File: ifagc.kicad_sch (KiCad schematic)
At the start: 39 parts, among them Q901 MMBFJ310, Q902 MMBFJ310, Q903 MMBT3904, Q904 MMBT3904, Q905 BSS138, T901 FT37-43

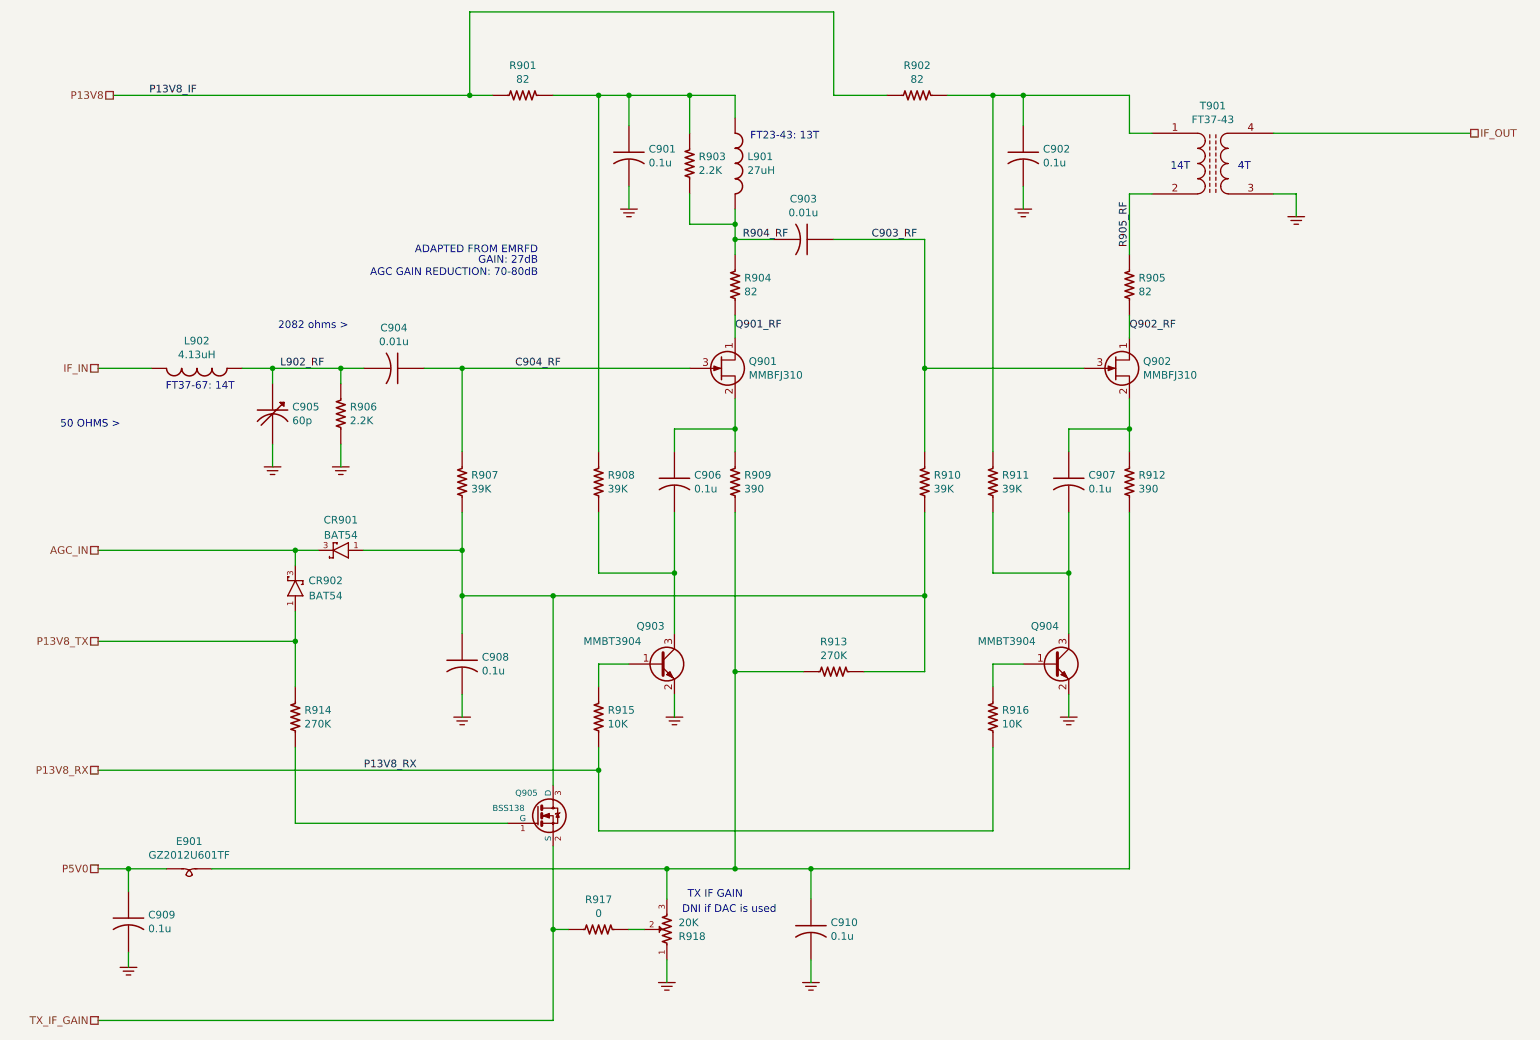
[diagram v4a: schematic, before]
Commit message: trx_mobo_concept_2_B. Change design to use a dedicated 8V supply for the 2SC3357 parts. Add S-Meter connector. Change mic connector to 3 pins and add 8V sopower supply to pin 3.
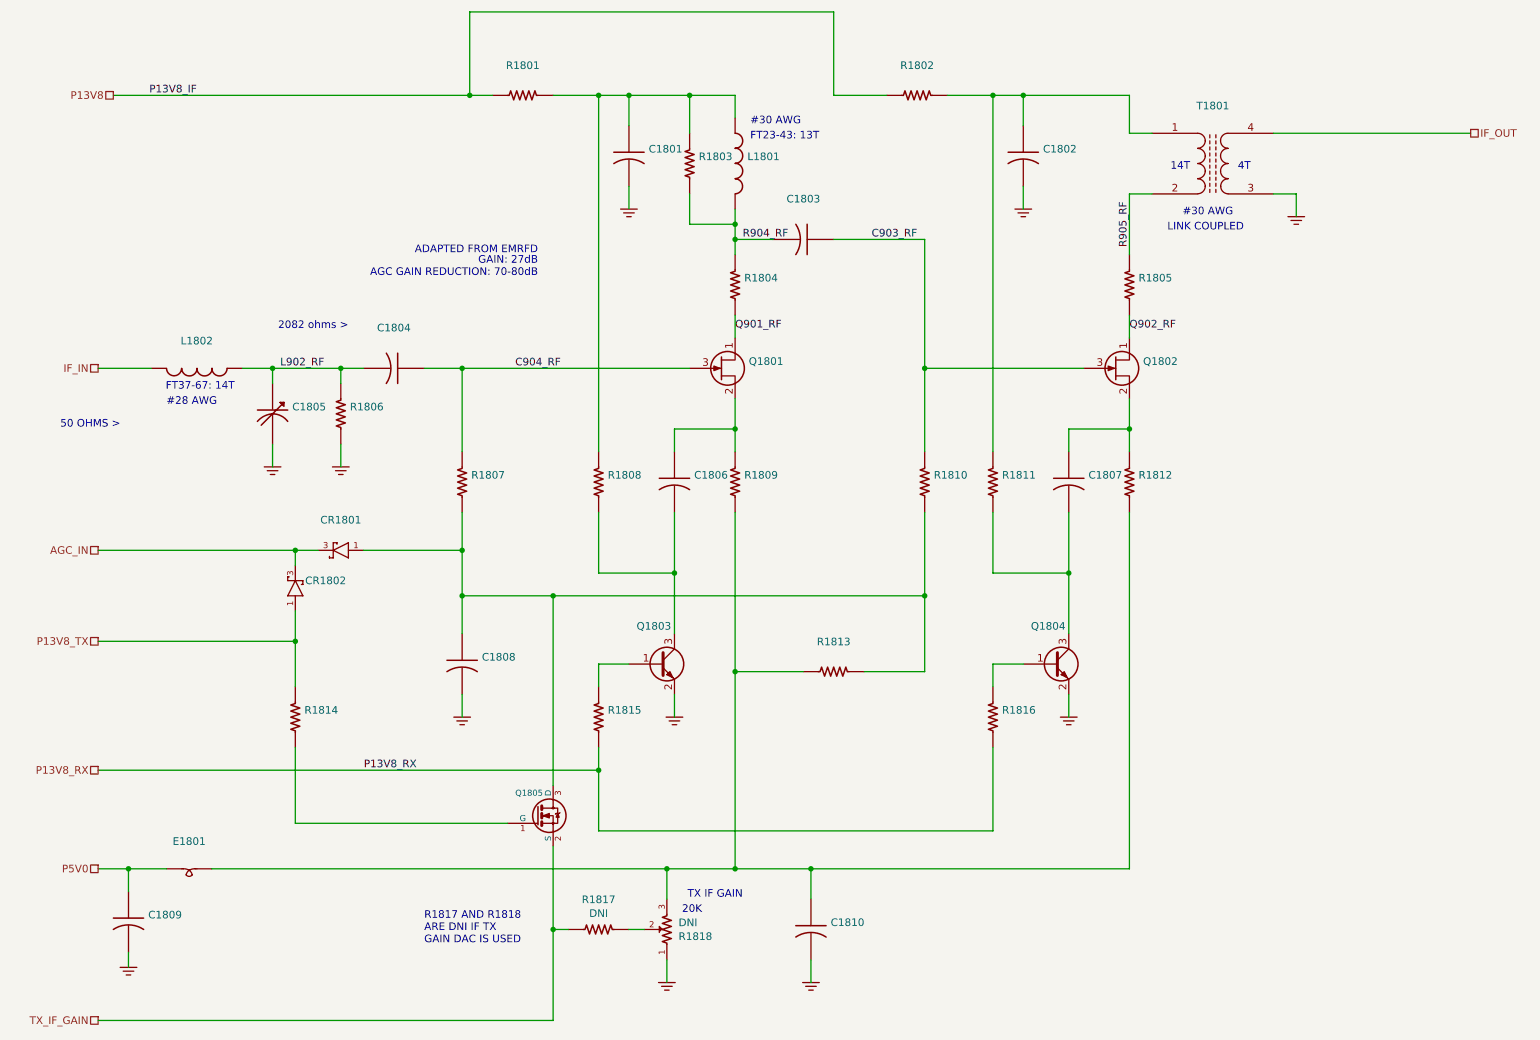
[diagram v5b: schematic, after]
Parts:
- C1801: renamed from C901; value 0.1u -> (none); footprint Capacitor_SMD:C_0805_2012Metric_Pad1.15x1.40mm_HandSolder -> (none)
- C1802: renamed from C902; value 0.1u -> (none); footprint Capacitor_SMD:C_0805_2012Metric_Pad1.15x1.40mm_HandSolder -> (none)
- C1803: renamed from C903; value 0.01u -> (none); footprint Capacitor_SMD:C_0805_2012Metric_Pad1.15x1.40mm_HandSolder -> (none)
- C1804: renamed from C904; value 0.01u -> (none); footprint Capacitor_SMD:C_0805_2012Metric_Pad1.15x1.40mm_HandSolder -> (none)
- C1805: renamed from C905; value 60p -> (none); footprint mods:Cap_Trimmer_THT_6mm_plastic -> (none)
- C1806: renamed from C906; value 0.1u -> (none); footprint Capacitor_SMD:C_0805_2012Metric_Pad1.15x1.40mm_HandSolder -> (none)
- C1807: renamed from C907; value 0.1u -> (none); footprint Capacitor_SMD:C_0805_2012Metric_Pad1.15x1.40mm_HandSolder -> (none)
- C1808: renamed from C908; value 0.1u -> (none); footprint Capacitor_SMD:C_0805_2012Metric_Pad1.15x1.40mm_HandSolder -> (none)
- C1809: renamed from C909; value 0.1u -> (none); footprint Capacitor_SMD:C_0805_2012Metric_Pad1.15x1.40mm_HandSolder -> (none)
- C1810: renamed from C910; value 0.1u -> (none); footprint Capacitor_SMD:C_0805_2012Metric_Pad1.15x1.40mm_HandSolder -> (none)
- CR1801: renamed from CR901; value BAT54 -> (none); footprint mods:SOT23-3-SAR -> (none)
- CR1802: renamed from CR902; value BAT54 -> (none); footprint mods:SOT23-3-SAR -> (none)
- E1801: renamed from E901; value GZ2012U601TF -> (none); footprint Inductor_SMD:L_0805_2012Metric -> (none)
- L1801: renamed from L901; value 27uH -> (none); footprint mods:IND_Handwound_FT23 -> (none); PartNumber 8000XX-XXX -> 800257-023
- L1802: renamed from L902; value 4.13uH -> (none); footprint mods:IND_Handwound_FT37 -> (none); PartNumber 8000XX-XXX -> 800307-101
- Q1801: renamed from Q901; value MMBFJ310 -> (none); footprint mods:SOT23-3-SAR -> (none)
- Q1802: renamed from Q902; value MMBFJ310 -> (none); footprint mods:SOT23-3-SAR -> (none)
- Q1803: renamed from Q903; value MMBT3904 -> (none); footprint mods:SOT23-3-SAR -> (none)
- Q1804: renamed from Q904; value MMBT3904 -> (none); footprint mods:SOT23-3-SAR -> (none)
- Q1805: renamed from Q905; value BSS138 -> (none); footprint mods:SOT23-3-SAR -> (none)
- R1801: renamed from R901; value 82 -> (none); footprint Resistor_SMD:R_0805_2012Metric_Pad1.15x1.40mm_HandSolder -> (none)
- R1802: renamed from R902; value 82 -> (none); footprint Resistor_SMD:R_0805_2012Metric_Pad1.15x1.40mm_HandSolder -> (none)
- R1803: renamed from R903; value 2.2K -> (none); footprint Resistor_SMD:R_0805_2012Metric_Pad1.15x1.40mm_HandSolder -> (none)
- R1804: renamed from R904; value 82 -> (none); footprint Resistor_SMD:R_0805_2012Metric_Pad1.15x1.40mm_HandSolder -> (none)
- R1805: renamed from R905; value 82 -> (none); footprint Resistor_SMD:R_0805_2012Metric_Pad1.15x1.40mm_HandSolder -> (none)
- R1806: renamed from R906; value 2.2K -> (none); footprint Resistor_SMD:R_0805_2012Metric_Pad1.15x1.40mm_HandSolder -> (none)
- R1807: renamed from R907; value 39K -> (none); footprint Resistor_SMD:R_0805_2012Metric_Pad1.15x1.40mm_HandSolder -> (none)
- R1808: renamed from R908; value 39K -> (none); footprint Resistor_SMD:R_0805_2012Metric_Pad1.15x1.40mm_HandSolder -> (none)
- R1809: renamed from R909; value 390 -> (none); footprint Resistor_SMD:R_0805_2012Metric_Pad1.15x1.40mm_HandSolder -> (none)
- R1810: renamed from R910; value 39K -> (none); footprint Resistor_SMD:R_0805_2012Metric_Pad1.15x1.40mm_HandSolder -> (none)
- R1811: renamed from R911; value 39K -> (none); footprint Resistor_SMD:R_0805_2012Metric_Pad1.15x1.40mm_HandSolder -> (none)
- R1812: renamed from R912; value 390 -> (none); footprint Resistor_SMD:R_0805_2012Metric_Pad1.15x1.40mm_HandSolder -> (none)
- R1813: renamed from R913; value 270K -> (none); footprint Resistor_SMD:R_0805_2012Metric_Pad1.15x1.40mm_HandSolder -> (none)
- R1814: renamed from R914; value 270K -> (none); footprint Resistor_SMD:R_0805_2012Metric_Pad1.15x1.40mm_HandSolder -> (none)
- R1815: renamed from R915; value 10K -> (none); footprint Resistor_SMD:R_0805_2012Metric_Pad1.15x1.40mm_HandSolder -> (none)
- R1816: renamed from R916; value 10K -> (none); footprint Resistor_SMD:R_0805_2012Metric_Pad1.15x1.40mm_HandSolder -> (none)
- R1817: renamed from R917; value 0 -> DNI; footprint Resistor_SMD:R_0805_2012Metric_Pad1.15x1.40mm_HandSolder -> (none)
- R1818: renamed from R918; value 20K -> DNI; footprint mods:Potentiometer_Bourns_3296W_Vertical_Screw_SS -> (none)
- T1801: renamed from T901; value FT37-43 -> (none); footprint mods:XFMR_Handwound_FT37 -> (none)
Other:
- note added: "#28 AWG"
- note added: "#30 AWG"
- note added: "20K"
- note added: "LINK COUPLED"
- note added: "R1817 AND R1818 ARE DNI IF TX GAIN DAC IS USED"
- note removed: "DNI if DAC is used"

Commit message: Fix 12.288MHz part number in schematic, regenerate BOM's.
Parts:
- R1817, R1818: value DNI -> (none)
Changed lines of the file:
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@@
       (effects (font (size 1.27 1.27)) (justify right))
     )
-    (property "Value" "DNI" (id 1) (at 125.1458 169.037 90)
+    (property "Value" "" (id 1) (at 125.1458 169.037 90)
       (effects (font (size 1.27 1.27)) (justify right))
     )
@@
     (in_bom yes) (on_board yes)
     (property "Reference" "R1817" (id 0) (at 111.76 165.1762 90))
-    (property "Value" "DNI" (id 1) (at 111.76 167.4876 90))
+    (property "Value" "" (id 1) (at 111.76 167.4876 90))
     (property "Footprint" "" (id 2) (at 111.76 170.18 0)
       (effects (font (size 1.524 1.524)) hide)
